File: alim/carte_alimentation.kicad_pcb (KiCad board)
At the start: 2 copper layers, 30 parts, among them J11 Conn_01x02_Male, J12 Conn_01x02_Male, J21 Conn_01x02_Male, J22 Conn_01x02_Male, J31 Conn_01x02_Male, J32 Conn_01x02_Male, J40 Conn_01x02_Male, J41 Conn_01x02_Male, J42 Conn_01x02_Male, J43 Conn_01x02_Male, J44 Conn_01x02_Male, U1 LM2576T-5, U2 LM2576T-5, U3 LM2576T-5

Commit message: retrait radiateur (pas besoin cf robot 2A), debut routage
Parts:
- moved C11 227.9 mm to (294.6, 62.2)
- moved C12 193.4 mm to (262.9, 110.5)
- moved C21 168.9 mm to (259.1, 85.1)
- moved D3 149.9 mm to (185.4, 142.2)
- moved D1 146.8 mm to (194.3, 92.7)
- moved C32 146.3 mm to (226.1, 120.7)
- moved U2 146.2 mm to (212.1, 83.8)
- moved C31 145.8 mm to (221.0, 102.9)
- moved C22 132.3 mm to (250.2, 55.9)
- moved D2 125.3 mm to (212.1, 92.7)
- moved U3 115.8 mm to (188.0, 132.1)
- moved U1 105.8 mm to (199.4, 83.8)
- moved J21 86.4 mm to (182.9, 24.1)
- moved J40 1.32 mm to (158.8, 154.9)
- moved J44 1.32 mm to (158.8, 81.3)
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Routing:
- net Net-(F41-Pad1): track 0.00 -> 35.8 mm
- net Net-(F41-Pad2): track 0.00 -> 30.4 mm
- net Net-(J40-Pad2): track 0.00 -> 10.2 mm
- net Net-(C31-Pad1): track 0.00 -> 7.62 mm
- net Net-(C11-Pad1): track 0.00 -> 5.00 mm
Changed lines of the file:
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@@
     (thickness 1.6)
     (drawings 0)
-    (tracks 0)
+    (tracks 13)
     (zones 0)
     (modules 30)
@@
   )
   (setup
-    (last_trace_width 0.25)
+    (last_trace_width 3)
+    (user_trace_width 3)
     (trace_clearance 0.2)
     (zone_clearance 0.508)
@@
   )
   (module Capacitor_THT:CP_Radial_D10.0mm_P5.00mm (layer F.Cu)
-    (at 66.909647 71.145001)
+    (at 294.64 62.23)
     (descr "CP, Radial series, Radial, pin pitch=5.00mm, , diameter=10mm, Electrolytic Capacitor")
     (tags "CP Radial series Radial pin pitch 5.00mm  diameter 10mm Electrolytic Capacitor")
@@
   )
   (module Capacitor_THT:CP_Radial_D10.0mm_P5.00mm (layer F.Cu)
-    (at 76.449647 59.235001)
+    (at 262.89 110.49)
     (descr "CP, Radial series, Radial, pin pitch=5.00mm, , diameter=10mm, Electrolytic Capacitor")
     (tags "CP Radial series Radial pin pitch 5.00mm  diameter 10mm Electrolytic Capacitor")
@@
   )
   (module Capacitor_THT:CP_Radial_D10.0mm_P5.00mm (layer F.Cu)
-    (at 93.099647 54.085001)
+    (at 259.08 85.09)
     (descr "CP, Radial series, Radial, pin pitch=5.00mm, , diameter=10mm, Electrolytic Capacitor")
     (tags "CP Radial series Radial pin pitch 5.00mm  diameter 10mm Electrolytic Capacitor")
@@
   )
   (module Capacitor_THT:CP_Radial_D10.0mm_P5.00mm (layer F.Cu)
-    (at 119.289647 37.025001)
+    (at 250.19 55.88)
     (descr "CP, Radial series, Radial, pin pitch=5.00mm, , diameter=10mm, Electrolytic Capacitor")
     (tags "CP Radial series Radial pin pitch 5.00mm  diameter 10mm Electrolytic Capacitor")
@@
   )
   (module Capacitor_THT:CP_Radial_D10.0mm_P5.00mm (layer F.Cu)
-    (at 78.719647 70.785001)
+    (at 220.98 102.87)
     (descr "CP, Radial series, Radial, pin pitch=5.00mm, , diameter=10mm, Electrolytic Capacitor")
     (tags "CP Radial series Radial pin pitch 5.00mm  diameter 10mm Electrolytic Capacitor")
@@
   )
   (module Capacitor_THT:CP_Radial_D10.0mm_P5.00mm (layer F.Cu)
-    (at 90.529647 65.635001)
+    (at 226.06 120.65)
     (descr "CP, Radial series, Radial, pin pitch=5.00mm, , diameter=10mm, Electrolytic Capacitor")
     (tags "CP Radial series Radial pin pitch 5.00mm  diameter 10mm Electrolytic Capacitor")
@@
   )
   (module Diode_THT:D_DO-27_P12.70mm_Horizontal (layer F.Cu)
-    (at 48.695001 73.965001)
+    (at 194.31 92.71)
     (descr "Diode, DO-27 series, Axial, Horizontal, pin pitch=12.7mm, , length*diameter=9.52*5.33mm^2, , http://www.slottechforum.com/slotinfo/Techstuff/CD2%20Diodes%20and%20Transistors/Cases/Diode%20DO-27.jpg")
     (tags "Diode DO-27 series Axial Horizontal pin pitch 12.7mm  length 9.52mm diameter 5.33mm")
@@
   )
   (module Diode_THT:D_DO-27_P12.70mm_Horizontal (layer F.Cu)
-    (at 101.075001 34.695001)
+    (at 212.09 92.71)
     (descr "Diode, DO-27 series, Axial, Horizontal, pin pitch=12.7mm, , length*diameter=9.52*5.33mm^2, , http://www.slottechforum.com/slotinfo/Techstuff/CD2%20Diodes%20and%20Transistors/Cases/Diode%20DO-27.jpg")
     (tags "Diode DO-27 series Axial Horizontal pin pitch 12.7mm  length 9.52mm diameter 5.33mm")
@@
   )
   (module Diode_THT:D_DO-27_P12.70mm_Horizontal (layer F.Cu)
-    (at 48.695001 80.855001)
+    (at 185.42 142.24)
     (descr "Diode, DO-27 series, Axial, Horizontal, pin pitch=12.7mm, , length*diameter=9.52*5.33mm^2, , http://www.slottechforum.com/slotinfo/Techstuff/CD2%20Diodes%20and%20Transistors/Cases/Diode%20DO-27.jpg")
     (tags "Diode DO-27 series Axial Horizontal pin pitch 12.7mm  length 9.52mm diameter 5.33mm")
@@
   )
   (module TerminalBlock:TerminalBlock_bornier-2_P5.08mm (layer F.Cu)
-    (at 104.605001 60.705001)
+    (at 182.88 24.13)
     (descr "simple 2-pin terminal block, pitch 5.08mm, revamped version of bornier2")
     (tags "terminal block bornier2")
@@
   )
   (module TerminalBlock:TerminalBlock_bornier-2_P5.08mm (layer F.Cu)
-    (at 160.075 154.94)
+    (at 158.75 154.94)
     (descr "simple 2-pin terminal block, pitch 5.08mm, revamped version of bornier2")
     (tags "terminal block bornier2")
@@
   )
   (module TerminalBlock:TerminalBlock_bornier-2_P5.08mm (layer F.Cu)
-    (at 160.02 69.85)
+    (at 158.75 69.85)
     (descr "simple 2-pin terminal block, pitch 5.08mm, revamped version of bornier2")
     (tags "terminal block bornier2")
@@
   )
   (module TerminalBlock:TerminalBlock_bornier-2_P5.08mm (layer F.Cu)
-    (at 160.075 81.28)
+    (at 158.75 81.28)
     (descr "simple 2-pin terminal block, pitch 5.08mm, revamped version of bornier2")
     (tags "terminal block bornier2")
@@
   )
   (module Package_TO_SOT_THT:TO-220F-5_P3.4x2.06mm_StaggerEven_Lead1.86mm_Vertical (layer F.Cu)
-    (at 101.605001 43.415001)
+    (at 199.39 83.82)
     (descr "TO-220F-5, Vertical, RM 1.7mm, PentawattF-, MultiwattF-5, staggered type-2")
     (tags "TO-220F-5 Vertical RM 1.7mm PentawattF- MultiwattF-5 staggered type-2")
@@
   )
   (module Package_TO_SOT_THT:TO-220F-5_P3.4x2.06mm_StaggerEven_Lead1.86mm_Vertical (layer F.Cu)
-    (at 65.875001 82.195001)
+    (at 212.09 83.82)
     (descr "TO-220F-5, Vertical, RM 1.7mm, PentawattF-, MultiwattF-5, staggered type-2")
     (tags "TO-220F-5 Vertical RM 1.7mm PentawattF- MultiwattF-5 staggered type-2")
@@
   )
   (module Package_TO_SOT_THT:TO-220F-5_P3.4x2.06mm_StaggerEven_Lead1.86mm_Vertical (layer F.Cu)
-    (at 103.875001 52.435001)
+    (at 187.96 132.08)
     (descr "TO-220F-5, Vertical, RM 1.7mm, PentawattF-, MultiwattF-5, staggered type-2")
     (tags "TO-220F-5 Vertical RM 1.7mm PentawattF- MultiwattF-5 staggered type-2")
@@
     )
   )
+  (segment (start 177.8 100.062) (end 177.8 95.062) (width 3) (layer B.Cu) (net 2))
+  (segment (start 163.865 139.7) (end 163.865 132.08) (width 3) (layer B.Cu) (net 5))
+  (segment (start 163.83 100.25) (end 163.83 95.25) (width 3) (layer B.Cu) (net 10))
+  (segment (start 163.83 69.85) (end 163.83 81.28) (width 3) (layer B.Cu) (net 10))
+  (segment (start 163.83 81.28) (end 163.83 95.25) (width 3) (layer B.Cu) (net 10))
+  (segment (start 163.83 110.25) (end 163.83 115.25) (width 3) (layer B.Cu) (net 11))
+  (segment (start 177.8 110.062) (end 177.8 115.062) (width 3) (layer B.Cu) (net 11))
+  (segment (start 164.018 115.062) (end 163.83 115.25) (width 3) (layer B.Cu) (net 11))
+  (segment (start 177.8 115.062) (end 164.018 115.062) (width 3) (layer B.Cu) (net 11))
+  (segment (start 163.83 126.965) (end 163.865 127) (width 3) (layer B.Cu) (net 11))
+  (segment (start 163.83 115.25) (end 163.83 126.965) (width 3) (layer B.Cu) (net 11))
+  (segment (start 163.865 154.905) (end 163.83 154.94) (width 3) (layer B.Cu) (net 12))
+  (segment (start 163.865 144.78) (end 163.865 154.905) (width 3) (layer B.Cu) (net 12))
 )

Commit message: routage
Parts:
- moved C11 231.3 mm to (63.5, 54.6), turned to 270 degrees
- moved C21 193.5 mm to (66.0, 72.4), turned to 270 degrees
- moved C31 161.3 mm to (59.7, 102.9), turned to 270 degrees
- moved C12 159.0 mm to (111.8, 61.0), turned to 90 degrees
- moved U1 137.8 mm to (67.3, 44.5)
- moved C22 136.5 mm to (118.1, 90.2), turned to 90 degrees
- moved U2 136.3 mm to (76.2, 73.7)
- moved F42 126.6 mm to (54.6, 85.9)
- moved F41 122.9 mm to (44.5, 66.0)
- moved J41 122.9 mm to (44.5, 110.5)
- moved J42 122.9 mm to (44.5, 97.8)
- moved U3 122.9 mm to (68.6, 102.9)
- moved J40 122.9 mm to (39.4, 125.7)
- moved J43 122.9 mm to (39.4, 40.6)
- moved J44 122.9 mm to (39.4, 52.1)
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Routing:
- net Net-(C32-Pad2): track 0.00 -> 73.1 mm
- net Net-(C22-Pad2): track 0.00 -> 66.2 mm
- net Net-(C11-Pad1): track 5.00 -> 56.0 mm
- net Net-(C12-Pad2): track 0.00 -> 50.4 mm
- net Net-(R11-Pad2): track 0.00 -> 36.6 mm
- net Net-(D2-Pad1): track 0.00 -> 26.7 mm
- net Net-(D3-Pad1): track 0.00 -> 26.5 mm
- net Net-(D1-Pad1): track 0.00 -> 25.1 mm
- net Net-(C31-Pad1): track 7.62 -> 31.7 mm
- net Net-(R11-Pad1): track 0.00 -> 7.18 mm
- net Net-(F41-Pad1): track 35.8 -> 38.4 mm
- added copper zone on B.Cu, net GND
- added copper zone on F.Cu, net GND

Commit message: et tu routes, routes, routes
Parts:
- added REF**: MountingHole_3.2mm_M3, MountingHole:MountingHole_3.2mm_M3, F.Cu at (54.6, 127.0)
- added REF**: MountingHole_3.2mm_M3, MountingHole:MountingHole_3.2mm_M3, F.Cu at (54.6, 40.6)
- added REF**: MountingHole_3.2mm_M3, MountingHole:MountingHole_3.2mm_M3, F.Cu at (143.5, 40.6)
- added REF**: MountingHole_3.2mm_M3, MountingHole:MountingHole_3.2mm_M3, F.Cu at (143.5, 127.0)
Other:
- board text added: "12V 3A"
- board text added: "5V 1.5A"
- board text added: "5V 3A"
- board text added: "Arret"
- board text added: "Mot"
- board text added: "Vbat"
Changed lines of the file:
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@@
   (general
     (thickness 1.6)
-    (drawings 2)
+    (drawings 8)
     (tracks 70)
     (zones 0)
-    (modules 30)
+    (modules 34)
     (nets 15)
   )
@@
     (add_net "Net-(R11-Pad1)")
     (add_net "Net-(R11-Pad2)")
+  )
+  (module MountingHole:MountingHole_3.2mm_M3 (layer F.Cu)
+    (at 54.61 127)
+    (descr "Mounting Hole 3.2mm, no annular, M3")
+    (tags "mounting hole 3.2mm no annular m3")
+    (attr virtual)
+    (fp_text reference REF** (at 0 -4.2) (layer F.SilkS)
+      (effects (font (size 1 1) (thickness 0.15)))
+    )
+    (fp_text value MountingHole_3.2mm_M3 (at 0 4.2) (layer F.Fab)
+      (effects (font (size 1 1) (thickness 0.15)))
+    )
+    (fp_circle (center 0 0) (end 3.45 0) (layer F.CrtYd) (width 0.05))
+    (fp_circle (center 0 0) (end 3.2 0) (layer Cmts.User) (width 0.15))
+    (fp_text user %R (at 0.3 0) (layer F.Fab)
+      (effects (font (size 1 1) (thickness 0.15)))
+    )
+    (pad 1 np_thru_hole circle (at 0 0) (size 3.2 3.2) (drill 3.2) (layers *.Cu *.Mask))
+  )
+  (module MountingHole:MountingHole_3.2mm_M3 (layer F.Cu)
+    (at 54.61 40.64)
+    (descr "Mounting Hole 3.2mm, no annular, M3")
+    (tags "mounting hole 3.2mm no annular m3")
+    (attr virtual)
+    (fp_text reference REF** (at 0 -4.2) (layer F.SilkS)
+      (effects (font (size 1 1) (thickness 0.15)))
+    )
+    (fp_text value MountingHole_3.2mm_M3 (at 0 4.2) (layer F.Fab)
+      (effects (font (size 1 1) (thickness 0.15)))
+    )
+    (fp_circle (center 0 0) (end 3.45 0) (layer F.CrtYd) (width 0.05))
+    (fp_circle (center 0 0) (end 3.2 0) (layer Cmts.User) (width 0.15))
+    (fp_text user %R (at 0.3 0) (layer F.Fab)
+      (effects (font (size 1 1) (thickness 0.15)))
+    )
+    (pad 1 np_thru_hole circle (at 0 0) (size 3.2 3.2) (drill 3.2) (layers *.Cu *.Mask))
+  )
+  (module MountingHole:MountingHole_3.2mm_M3 (layer F.Cu)
+    (at 143.51 40.64)
+    (descr "Mounting Hole 3.2mm, no annular, M3")
+    (tags "mounting hole 3.2mm no annular m3")
+    (attr virtual)
+    (fp_text reference REF** (at 0 -4.2) (layer F.SilkS)
+      (effects (font (size 1 1) (thickness 0.15)))
+    )
+    (fp_text value MountingHole_3.2mm_M3 (at 0 4.2) (layer F.Fab)
+      (effects (font (size 1 1) (thickness 0.15)))
+    )
+    (fp_circle (center 0 0) (end 3.45 0) (layer F.CrtYd) (width 0.05))
+    (fp_circle (center 0 0) (end 3.2 0) (layer Cmts.User) (width 0.15))
+    (fp_text user %R (at 0.3 0) (layer F.Fab)
+      (effects (font (size 1 1) (thickness 0.15)))
+    )
+    (pad 1 np_thru_hole circle (at 0 0) (size 3.2 3.2) (drill 3.2) (layers *.Cu *.Mask))
+  )
+  (module MountingHole:MountingHole_3.2mm_M3 (layer F.Cu)
+    (at 143.51 127)
+    (descr "Mounting Hole 3.2mm, no annular, M3")
+    (tags "mounting hole 3.2mm no annular m3")
+    (attr virtual)
+    (fp_text reference REF** (at 0 -4.2) (layer F.SilkS)
+      (effects (font (size 1 1) (thickness 0.15)))
+    )
+    (fp_text value MountingHole_3.2mm_M3 (at 0 4.2) (layer F.Fab)
+      (effects (font (size 1 1) (thickness 0.15)))
+    )
+    (fp_circle (center 0 0) (end 3.45 0) (layer F.CrtYd) (width 0.05))
+    (fp_circle (center 0 0) (end 3.2 0) (layer Cmts.User) (width 0.15))
+    (fp_text user %R (at 0.3 0) (layer F.Fab)
+      (effects (font (size 1 1) (thickness 0.15)))
+    )
+    (pad 1 np_thru_hole circle (at 0 0) (size 3.2 3.2) (drill 3.2) (layers *.Cu *.Mask))
   )
   (module Capacitor_THT:CP_Radial_D10.0mm_P5.00mm (layer F.Cu)
@@
     )
   )
+  (gr_text "5V 1.5A" (at 137.16 123.19) (layer F.Cu)
+    (effects (font (size 1 1) (thickness 0.15)))
+  )
+  (gr_text "5V 3A" (at 137.16 96.52) (layer F.Cu)
+    (effects (font (size 1 1) (thickness 0.15)))
+  )
+  (gr_text "12V 3A" (at 135.89 67.31) (layer F.Cu)
+    (effects (font (size 1 1) (thickness 0.15)))
+  )
+  (gr_text Mot (at 50.8 46.99) (layer F.Cu)
+    (effects (font (size 1 1) (thickness 0.15)))
+  )
+  (gr_text "Arret\n" (at 53.34 97.79) (layer F.Cu)
+    (effects (font (size 1 1) (thickness 0.15)))
+  )
+  (gr_text Vbat (at 49.53 123.19) (layer F.Cu)
+    (effects (font (size 1 1) (thickness 0.15)))
+  )
   (dimension 99.06 (width 0.12) (layer F.SilkS)

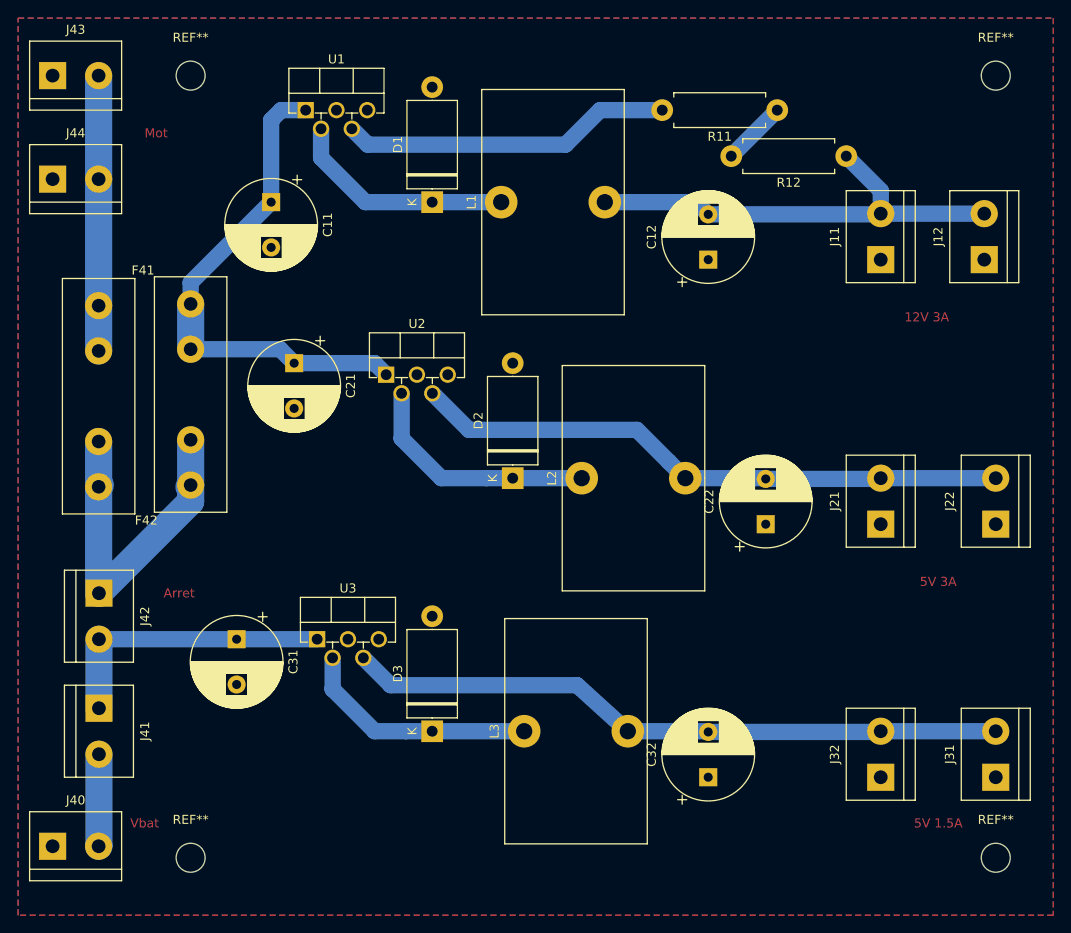
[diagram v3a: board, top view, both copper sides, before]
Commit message: correction polarisation condensateur, ajout texte, compactage verif rapide boucle de courant
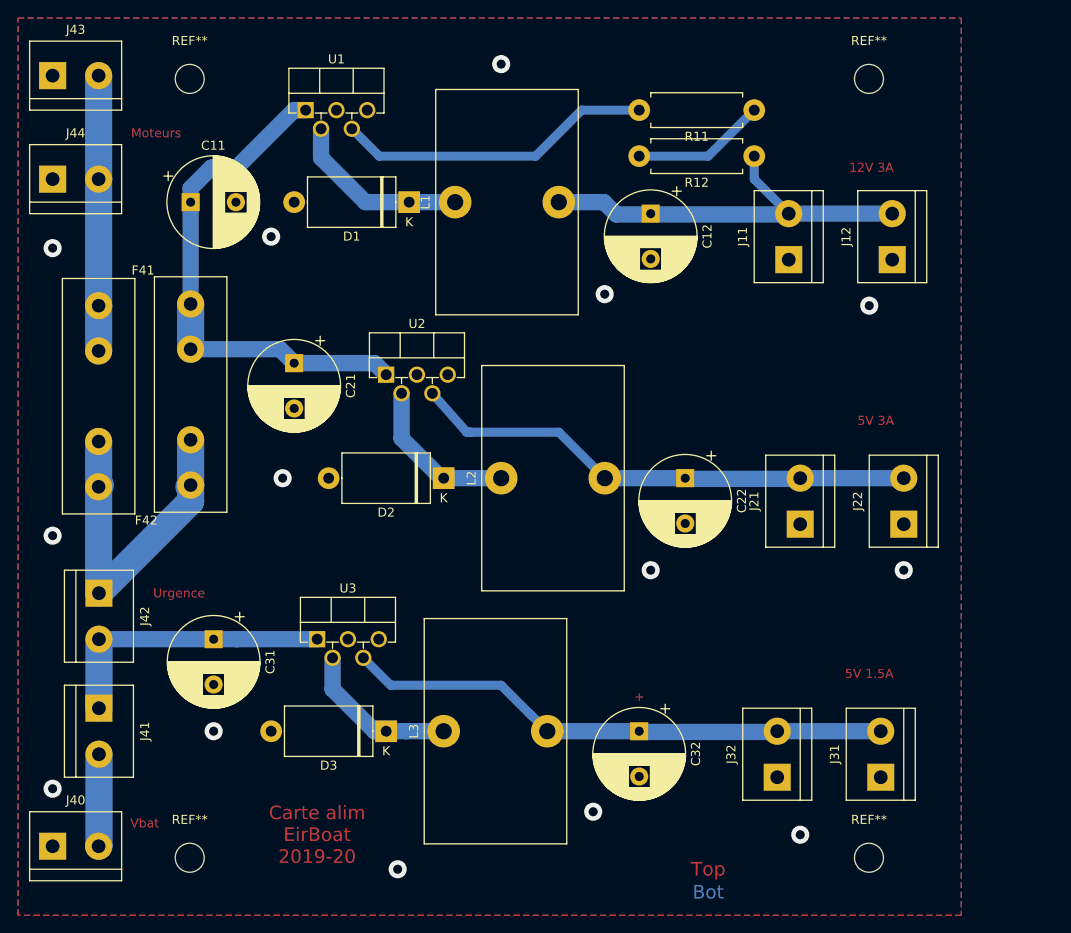
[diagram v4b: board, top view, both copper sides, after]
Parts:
- moved REF** 14.0 mm to (129.5, 41.0)
- moved REF** 14.0 mm to (129.5, 127.0)
- moved J31 12.7 mm to (130.8, 118.1)
- moved J32 11.4 mm to (119.4, 118.1)
- moved C22 10.2 mm to (109.2, 85.1), turned to 270 degrees
- moved J11 10.2 mm to (120.7, 61.0)
- moved J12 10.2 mm to (132.1, 61.0)
- moved J22 10.2 mm to (133.3, 90.2)
- moved R12 10.2 mm to (116.8, 49.5)
- moved C32 9.16 mm to (104.1, 113.0), turned to 270 degrees
- moved C11 8.89 mm to (54.6, 54.6), turned to 0 degrees
- moved J21 8.89 mm to (121.9, 90.2)
- moved L2 8.89 mm to (88.9, 85.1)
- moved L3 8.89 mm to (82.5, 113.0)
- moved C12 8.13 mm to (105.4, 55.9), turned to 270 degrees
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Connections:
- C12 pad 1: GND -> Net-(C12-Pad1)
- C12 pad 2: Net-(C12-Pad2) -> GND
- C22 pad 1: GND -> Net-(C22-Pad1)
- C22 pad 2: Net-(C22-Pad2) -> GND
- C32 pad 1: GND -> Net-(C32-Pad1)
- C32 pad 2: Net-(C32-Pad2) -> GND
- J11 pad 2: Net-(C12-Pad2) -> Net-(C12-Pad1)
- J12 pad 2: Net-(C12-Pad2) -> Net-(C12-Pad1)
- J21 pad 2: Net-(C22-Pad2) -> Net-(C22-Pad1)
- J22 pad 2: Net-(C22-Pad2) -> Net-(C22-Pad1)
- J31 pad 2: Net-(C32-Pad2) -> Net-(C32-Pad1)
- J32 pad 2: Net-(C32-Pad2) -> Net-(C32-Pad1)
- L1 pad 2: Net-(C12-Pad2) -> Net-(C12-Pad1)
- L2 pad 2: Net-(C22-Pad2) -> Net-(C22-Pad1)
- L3 pad 2: Net-(C32-Pad2) -> Net-(C32-Pad1)
- R12 pad 1: Net-(C12-Pad2) -> Net-(C12-Pad1)
- U2 pad 4: Net-(C22-Pad2) -> Net-(C22-Pad1)
- U3 pad 4: Net-(C32-Pad2) -> Net-(C32-Pad1)
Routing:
- net Net-(C32-Pad2): track 73.1 -> 0.00 mm
- net Net-(C22-Pad2): track 66.2 -> 0.00 mm
- net Net-(C32-Pad1): track 0.00 -> 60.6 mm
- net Net-(C22-Pad1): track 0.00 -> 56.7 mm
- net Net-(C12-Pad2): track 50.4 -> 0.00 mm
- net Net-(C12-Pad1): track 0.00 -> 45.3 mm
- net Net-(D2-Pad1): track 26.7 -> 17.5 mm
- net Net-(D3-Pad1): track 26.5 -> 17.6 mm
- net Net-(R11-Pad1): track 7.18 -> 14.8 mm
- net Net-(D1-Pad1): track 25.1 -> 20.0 mm
- net Net-(R11-Pad2): track 36.6 -> 35.1 mm
- net Net-(C11-Pad1): track 56.0 -> 56.8 mm
- net GND: vias 0 -> 14
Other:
- board text added: "+"
- board text added: "Bot"
- board text added: "Carte alim EirBoat 2019-20"
- board text added: "Moteurs"
- board text added: "Top"
- board text added: "Urgence"
- board text removed: "Arret"
- board text removed: "Mot"

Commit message: retrait arret general, il sera entre la batterie et la carte de secu
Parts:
- removed J41: Conn_01x02_Male, TerminalBlock:TerminalBlock_bornier-2_P5.08mm
- moved J40 7.62 mm to (39.4, 118.1)
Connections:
- J40 pad 2: Net-(J40-Pad2) -> Net-(C31-Pad1)
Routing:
- net Net-(J40-Pad2): track 10.2 -> 0.00 mm
- net Net-(C31-Pad1): track 31.7 -> 39.3 mm
